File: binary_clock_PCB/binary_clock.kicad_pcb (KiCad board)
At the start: 4 copper layers, 250 x 25 mm, 73 parts, among them J1 USB4105-GF-A, J2 uFL, J3 Conn_01x08_Socket, J4 JST-SM04B-SRSS, J5 JST-SM04B-SRSS, J6 JST-SM04B-SRSS, SW1 PTS636 SK25F, SW2 PTS636 SK25F, U1 ESP32-S3-WROOM-2-N32R8V, U2 AP2112K-3.3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

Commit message: fghxfhxcfhxfhgxfgh sxrfhxfr v
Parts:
- moved NEO VBUS 9.74 mm to (274.1, 52.4), turned to 90 degrees
- moved C6 4.71 mm to (115.9, 58.6)
- moved U5 4.70 mm to (122.8, 56.2)
- moved U4 4.70 mm to (101.9, 56.2)
- moved J2 4.70 mm to (110.5, 52.9)
- moved U6 3.71 mm to (153.6, 60.6)
- moved C7 3.50 mm to (152.9, 61.9)
- moved C27 3.35 mm to (273.2, 48.4)
- moved D20 3.32 mm to (271.5, 44.6)
- moved C26 3.14 mm to (259.2, 48.3)
- moved D19 3.14 mm to (257.6, 44.7)
- moved D18 2.97 mm to (243.6, 44.7)
- moved C25 2.97 mm to (245.3, 48.3)
- moved D17 2.81 mm to (229.7, 44.7)
- moved C24 2.81 mm to (231.3, 48.3)
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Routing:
- net /PPS: track 63.7 -> 59.1 mm
- net 3V3: track 208.2 -> 203.8 mm
- net VBUS: track 230.1 -> 231.9 mm

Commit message: dead :pensive:
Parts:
- JP3: renamed from NEO VBUS
- moved U7 34.5 mm to (56.9, 46.8), turned to -90 degrees
- moved R2 7.80 mm to (80.3, 60.3)
- moved R1 7.60 mm to (82.4, 60.3)
- moved J4 4.70 mm to (142.2, 56.2)
- moved C9 4.70 mm to (138.0, 54.9)
- moved JP3 1.35 mm to (274.1, 53.7)
- moved C7 0.20 mm to (153.1, 61.9)
- moved C15 0.05 mm to (105.9, 48.3)
- moved C16 0.05 mm to (119.8, 48.3)
- moved C19 0.05 mm to (161.6, 48.3)
- moved C20 0.05 mm to (175.6, 48.3)
- moved C21 0.05 mm to (189.5, 48.3)
- moved C22 0.05 mm to (203.5, 48.3)
- moved C23 0.05 mm to (217.4, 48.3)
- moved C24 0.05 mm to (231.4, 48.3)
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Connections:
- C10 pad 2: VBUS -> NEO_VBUS
- C11 pad 2: VBUS -> NEO_VBUS
- C12 pad 2: VBUS -> NEO_VBUS
- C13 pad 2: VBUS -> NEO_VBUS
- C14 pad 2: VBUS -> NEO_VBUS
- C15 pad 2: VBUS -> NEO_VBUS
- C16 pad 2: VBUS -> NEO_VBUS
- C17 pad 2: VBUS -> NEO_VBUS
- C18 pad 2: VBUS -> NEO_VBUS
- C19 pad 2: VBUS -> NEO_VBUS
- C20 pad 2: VBUS -> NEO_VBUS
- C21 pad 2: VBUS -> NEO_VBUS
- C22 pad 2: VBUS -> NEO_VBUS
- C23 pad 2: VBUS -> NEO_VBUS
- C24 pad 2: VBUS -> NEO_VBUS
- C25 pad 2: VBUS -> NEO_VBUS
- C26 pad 2: VBUS -> NEO_VBUS
- C27 pad 2: VBUS -> NEO_VBUS
- D10 pad 3: VBUS -> NEO_VBUS
- D11 pad 3: VBUS -> NEO_VBUS
- D12 pad 3: VBUS -> NEO_VBUS
- D13 pad 3: VBUS -> NEO_VBUS
- D14 pad 3: VBUS -> NEO_VBUS
- D15 pad 3: VBUS -> NEO_VBUS
- D16 pad 3: VBUS -> NEO_VBUS
- D17 pad 3: VBUS -> NEO_VBUS
- D18 pad 3: VBUS -> NEO_VBUS
- D19 pad 3: VBUS -> NEO_VBUS
- D20 pad 3: VBUS -> NEO_VBUS
- D3 pad 3: VBUS -> NEO_VBUS
- D4 pad 3: VBUS -> NEO_VBUS
- D5 pad 3: VBUS -> NEO_VBUS
- D6 pad 3: VBUS -> NEO_VBUS
- D7 pad 3: VBUS -> NEO_VBUS
- D8 pad 3: VBUS -> NEO_VBUS
- D9 pad 3: VBUS -> NEO_VBUS
- JP3 pad 2: VBUS -> NEO_VBUS
- U1 pad 15: unconnected-(U1-IO3-Pad15) -> /NEO_DISP
- U1 pad 31: /NEO_DISP -> /3V3_EN
- U3 pad 3: VBUS -> /3V3_EN
- U7 pad 1: 3V3 -> 3V3_MCU
- U7 pad 5: VBUS -> NEO_VBUS
- U7 pad 6: VBUS -> NEO_VBUS
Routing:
- net NEO_VBUS: track 0.00 -> 301.4 mm, vias 0 -> 1
- net /3V3_EN: track 0.00 -> 50.0 mm, vias 0 -> 2
- net /NEO_DISP: track 44.8 -> 4.66 mm
- net /NEO_5VLL: track 0.00 -> 33.1 mm, vias 0 -> 1
- net VBUS: track 231.9 -> 241.5 mm, vias 0 -> 1
- net /SDA: track 198.2 -> 194.1 mm
- net /SCL: track 199.7 -> 195.7 mm
- net 3V3: track 203.8 -> 199.8 mm
- net 3V3_MCU: track 64.1 -> 68.0 mm, vias 4 -> 6
- net /RESET: track 39.1 -> 37.3 mm
- net /RSR_SCL: track 8.62 -> 7.83 mm
- net /PPS: track 59.1 -> 59.8 mm
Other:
- board text added: "Bring out EN signal to 3V3 near I2C lines"
- board text removed: "3V3"
- board text removed: "Delete second LDO and swap RTC and GPS positions"

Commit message: Add gerber files
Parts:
- moved Boot 0.25 mm to (74.9, 54.0)
- moved C1 0.20 mm to (37.0, 40.8)
- moved C27 0.10 mm to (273.2, 48.3)
- moved D20 0.10 mm to (271.6, 44.7)
- moved C17 0.05 mm to (133.7, 48.3)
- renumbered SW1 to Boot
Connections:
- U1 pad 23: unconnected-(U1-IO21-Pad23) -> /ALM
- U5 pad 3: unconnected-(U5-~{INT}/SQW-Pad3) -> /ALM
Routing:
- net /ALM: track 0.00 -> 68.8 mm, vias 0 -> 2
- net GND: track 59.0 -> 106.4 mm, vias 50 -> 276
- net Net-(D4-DOUT): track 0.00 -> 10.9 mm
- net Net-(D5-DOUT): track 0.00 -> 10.9 mm
- net Net-(D19-DOUT): track 0.00 -> 10.4 mm
- net Net-(D18-DOUT): track 0.00 -> 10.4 mm
- net Net-(D17-DOUT): track 0.00 -> 10.4 mm
- net Net-(D16-DOUT): track 0.00 -> 10.4 mm
- net Net-(D10-DIN): track 0.00 -> 10.4 mm
- net Net-(D8-DOUT): track 0.00 -> 10.4 mm
- net Net-(D7-DOUT): track 0.00 -> 10.4 mm
- net Net-(D6-DOUT): track 0.00 -> 10.4 mm
- net Net-(D3-DOUT): track 0.00 -> 10.4 mm
- net Net-(D11-DOUT): track 0.00 -> 10.4 mm
- net Net-(D10-DOUT): track 0.00 -> 10.4 mm
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- added copper zone on B.Cu, net GND
- added copper zone on F.Cu, net GND
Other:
- rule pad_to_mask_clearance: 0.04 -> 0
- board text added: "3V3"
- board text added: "5V5"
- board text added: "ANT"
- board text added: "Binary Neopixel Clock"
- board text added: "Boot"
- board text added: "I2C"
- board text added: "IO10"
- board text added: "IO11"
- board text added: "IO12"
- board text added: "IO13"
- board text added: "IO14"
- board text added: "JLCJLCJLCJLC"
- board text added: "R1 3/23"
- board text added: "Reset"
- board text removed: "10"
- board text removed: "11"
- board text removed: "12"
- board text removed: "13"
- board text removed: "14"
- board text removed: "Board Flipped"
- board text removed: "Bring out EN signal to 3V3 near I2C lines"
- board text removed: "Hours"
- board text removed: "Minutes"
- board text removed: "Seconds"
- board text removed: "USB"
- board text removed: "https://youtu.be/PlXd3lLZ4vc?si=FWp1M6_FGoRUhZ_F&t=8296 2:18:16 have power and ground layers on top and bottom"
- board text removed: "remap schematic so pins are more accessible"

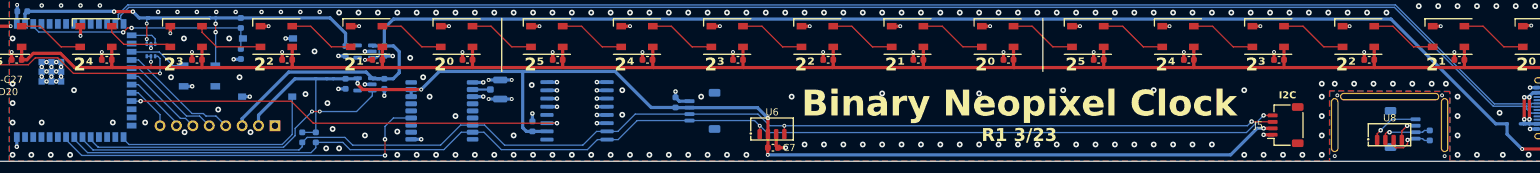
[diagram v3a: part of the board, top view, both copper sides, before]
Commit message: Fix silkscreen part designators
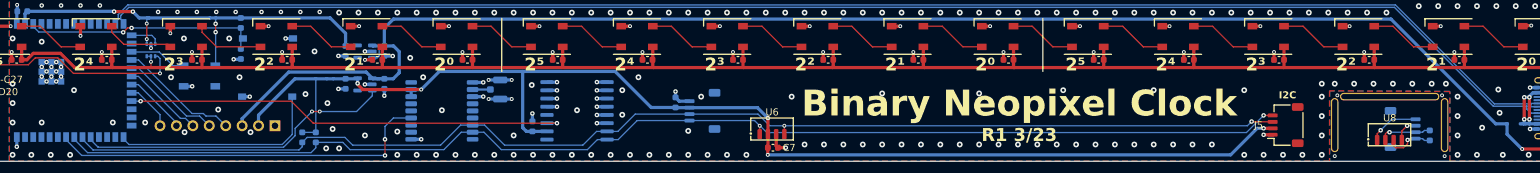
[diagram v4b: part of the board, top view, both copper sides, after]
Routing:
- net GND: vias 276 -> 281
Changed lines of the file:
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@@
 			(psnegative no)
 			(psa4output no)
-			(plotreference no)
+			(plotreference yes)
 			(plotvalue no)
 			(plotfptext yes)
@@
 	)
 	(via
+		(at 265.3 52.9)
+		(size 0.9)
+		(drill 0.4)
+		(layers "F.Cu" "B.Cu")
+		(free yes)
+		(net 2)
+	)
+	(via
 		(at 35.5 45)
 		(size 0.9)
@@
 	)
 	(via
+		(at 101.9 56.1)
+		(size 0.9)
+		(drill 0.4)
+		(layers "F.Cu" "B.Cu")
+		(free yes)
+		(net 2)
+	)
+	(via
 		(at 90 60)
 		(size 0.9)
@@
 	)
 	(via
+		(at 140 59.3)
+		(size 0.9)
+		(drill 0.4)
+		(layers "F.Cu" "B.Cu")
+		(free yes)
+		(net 2)
+	)
+	(via
 		(at 83 40.9)
 		(size 0.7)
@@
 	)
 	(via
+		(at 132.3 51)
+		(size 0.9)
+		(drill 0.4)
+		(layers "F.Cu" "B.Cu")
+		(free yes)
+		(net 2)
+	)
+	(via
 		(at 228.5 43.1)
 		(size 0.6)
@@
 	)
 	(via
+		(at 40 45.5)
+		(size 0.9)
+		(drill 0.4)
+		(layers "F.Cu" "B.Cu")
+		(free yes)
+		(net 2)
+	)
+	(via
 		(at 255 52)
 		(size 0.9)
@@
 	)
 	(via
+		(at 122.8 56.1)
+		(size 0.9)
+		(drill 0.4)
+		(layers "F.Cu" "B.Cu")
+		(free yes)
+		(net 2)
+	)
+	(via
 		(at 108.3 51.791375)
 		(size 0.7)
@@
 	)
 	(via
-		(at 100 54)
-		(size 0.9)
-		(drill 0.4)
-		(layers "F.Cu" "B.Cu")
-		(free yes)
-		(net 2)
-	)
-	(via
 		(at 117 43.1)
 		(size 0.6)
@@
 	)
 	(via
-		(at 104 57)
-		(size 0.9)
-		(drill 0.4)
-		(layers "F.Cu" "B.Cu")
-		(free yes)
-		(net 2)
-	)
-	(via
 		(at 158.8 43.1)
 		(size 0.6)
@@
 		(layers "F.Cu" "B.Cu")
 		(free yes)
+		(net 2)
+	)
+	(via
+		(at 262.8 58.8)
+		(size 0.9)
+		(drill 0.4)
+		(layers "F.Cu" "B.Cu")
+		(free yes)

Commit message: Fix minor bugs, improve holes
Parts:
- moved REF** 0.90 mm to (240.0, 59.3)
- moved REF** 0.90 mm to (257.0, 59.3)
- moved REF** 0.70 mm to (248.5, 54.7)
- moved J6 0.46 mm to (250.3, 59.4)
- moved C28 0.46 mm to (254.5, 60.4)
- moved U8 0.46 mm to (248.9, 61.9)
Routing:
- net GND: track 106.4 -> 106.3 mm, vias 281 -> 282
- net (no net): vias 4 -> 2
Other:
- board text added: "R2 4/24"
- board text removed: "R1 3/23"
